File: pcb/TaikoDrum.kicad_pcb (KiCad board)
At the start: 2 copper layers, 50 x 45 mm, 34 parts, among them J1 USB_B_Micro, J2 Conn_02x04_Odd_Even, U1 STM32F103C8Tx, U3 LM358, U4 LM3940IMPX-3.3_NOPB, Y1 8Mhz

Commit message: Added docs. Modified README.
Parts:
- moved J1 0.18 mm to (105.0, 140.4)
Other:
- board text added: "GND"
- board text added: "P1"
- board text added: "P2"
- board text added: "P3"
- board text added: "P4"
- board text added: "SWCLK"
- board text added: "SWDIO"
- board text added: "VCC"

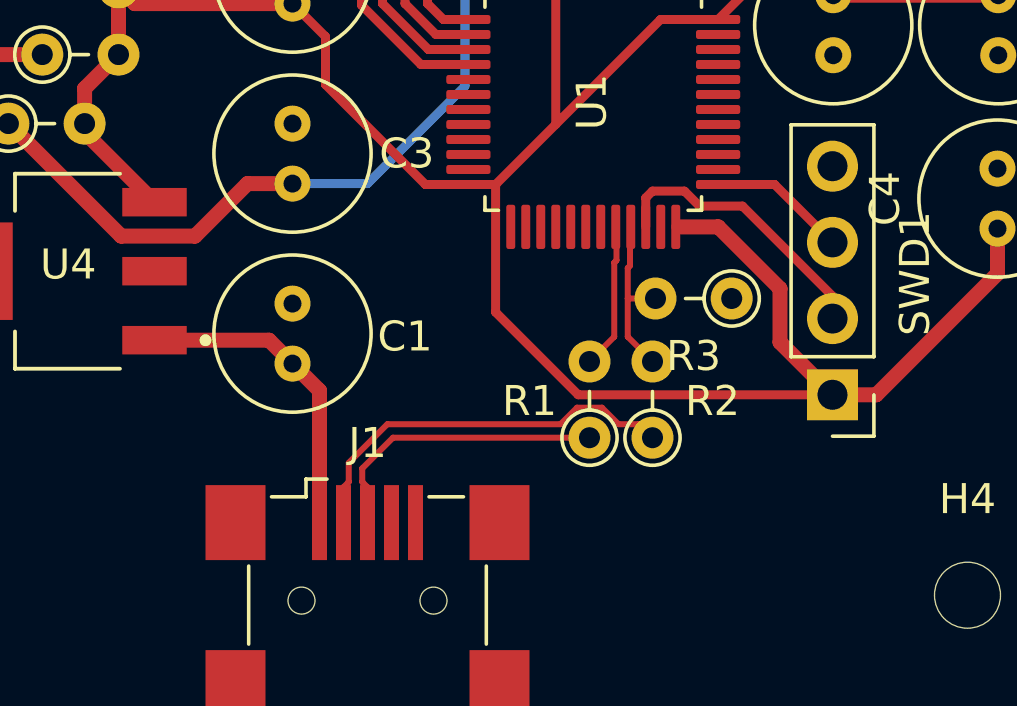
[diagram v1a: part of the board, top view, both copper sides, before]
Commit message: Fixed wrong USB wiring. Removed unecessary marks.
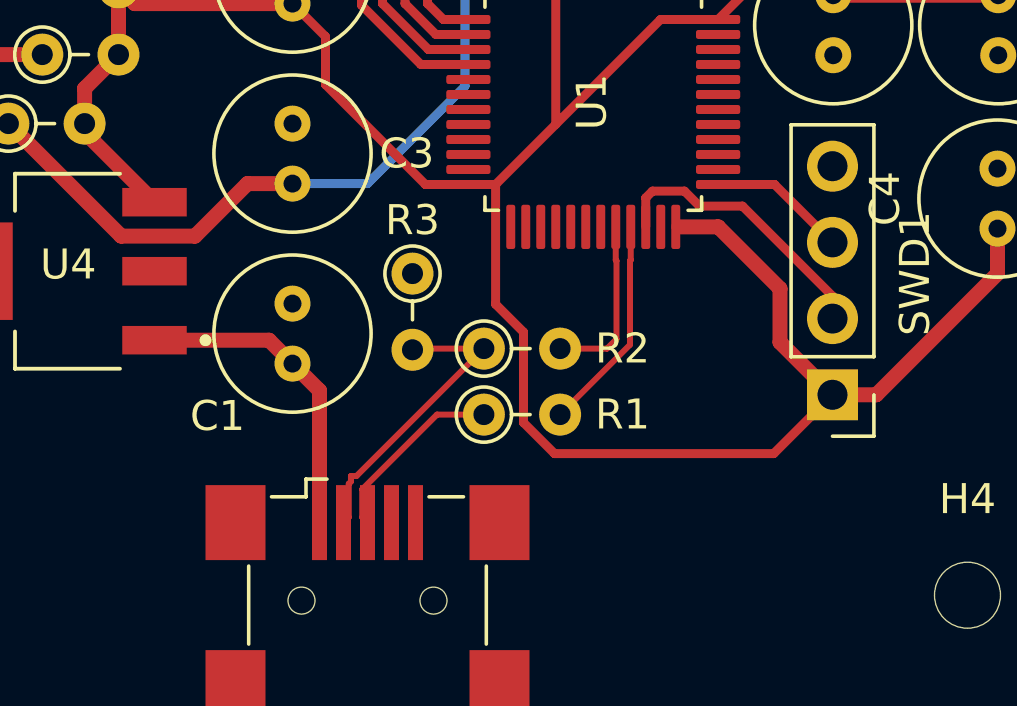
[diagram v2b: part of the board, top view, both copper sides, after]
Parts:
- R9: value 16M -> 1M
- moved R3 10.7 mm to (106.5, 129.5), turned to -90 degrees
- moved R2 6.36 mm to (108.9, 132.0), turned to 0 degrees
- moved R1 3.60 mm to (108.9, 134.2), turned to 0 degrees
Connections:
- U1 pad 32: D+ -> D-
- U1 pad 33: D- -> D+
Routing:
- net +3.3V: track 87.8 -> 91.0 mm
- net D-: track 19.0 -> 16.6 mm

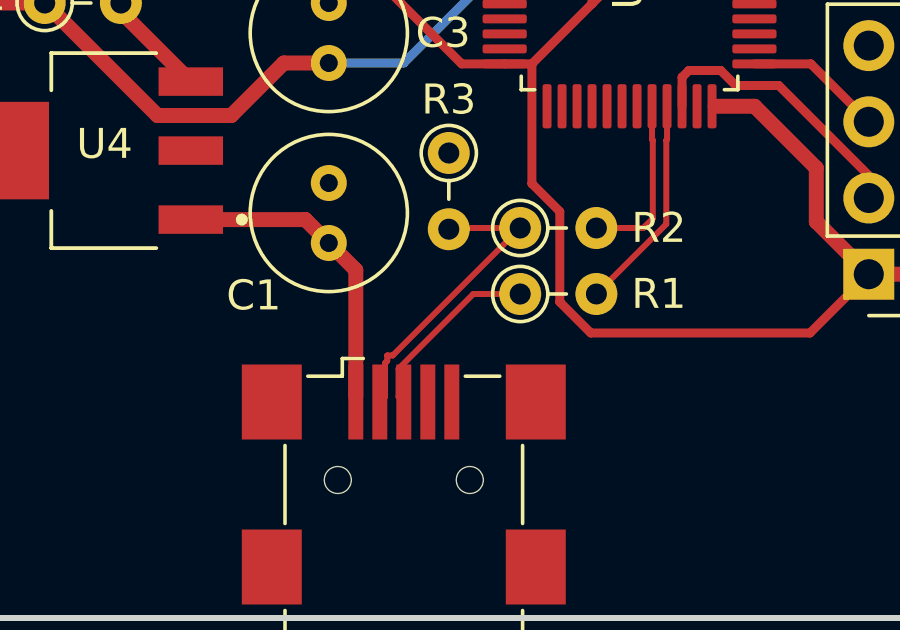
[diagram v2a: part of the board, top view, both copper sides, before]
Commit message: Better diff line routing. Additional dev text.
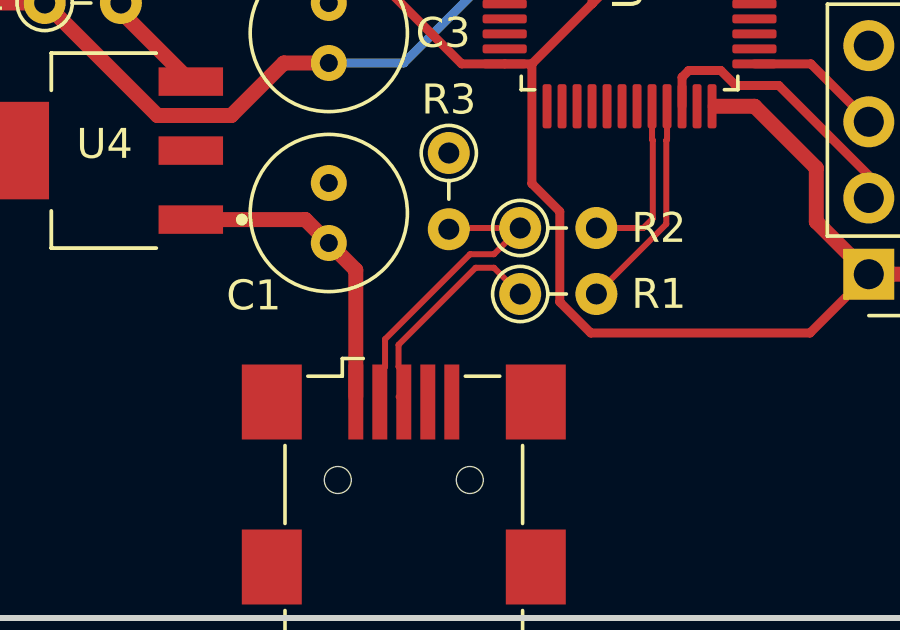
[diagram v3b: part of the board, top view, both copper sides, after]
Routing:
- net D+: track 14.1 -> 15.6 mm
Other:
- board text added: "USB-Micro-B"
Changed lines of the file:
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@@
 	)
 	(gr_text "VCC"
-		(at 125.2 134.1 0)
+		(at 118.6 134.2 0)
 		(layer "B.SilkS")
 		(effects
@@
 	)
 	(gr_text "SWDIO"
-		(at 126.8 129 0)
+		(at 118.6 129 0)
 		(layer "B.SilkS")
 		(effects
@@
 	)
 	(gr_text "GND"
-		(at 125.3 126.5 0)
+		(at 118.6 126.4 0)
 		(layer "B.SilkS")
 		(effects
@@
 	)
 	(gr_text "SWCLK"
-		(at 127.2 131.7 0)
+		(at 118.7 131.6 0)
+		(layer "B.SilkS")
+		(effects
+			(font
+				(size 1 1)
+				(thickness 0.1)
+			)
+			(justify left bottom mirror)
+		)
+	)
+	(gr_text "USB-Micro-B"
+		(at 110.2 143.2 0)
 		(layer "B.SilkS")
 		(effects
@@
 	)
 	(segment
+		(start 105 136.8)
+		(end 104.825 136.625)
+		(width 0.2)
+		(layer "F.Cu")
+		(net 9)
+	)
+	(segment
 		(start 113.75 129.073751)
 		(end 113.775 129.048751)
@@
 	)
 	(segment
-		(start 107.316397 134.2)
-		(end 108.88 134.2)
-		(width 0.2)
-		(layer "F.Cu")
-		(net 9)
-	)
-	(segment
 		(start 105 137.8)
 		(end 104.825001 137.625001)
@@
 	)
 	(segment
+		(start 105 137.8)
+		(end 105 136.8)
+		(width 0.2)
+		(layer "F.Cu")
+		(net 9)
+	)
+	(segment
+		(start 107.393197 133.325001)
+		(end 108.005001 133.325001)
+		(width 0.2)
+		(layer "F.Cu")
+		(net 9)
+	)
+	(segment
+		(start 108.005001 133.325001)
+		(end 108.88 134.2)
+		(width 0.2)
+		(layer "F.Cu")
+		(net 9)
+	)
+	(segment
+		(start 104.825 135.893198)
+		(end 107.393197 133.325001)
+		(width 0.2)
+		(layer "F.Cu")
+		(net 9)
+	)
+	(segment
 		(start 111.42 134.2)
 		(end 113.75 131.87)
@@
 	)
 	(segment
-		(start 104.825001 136.691396)
-		(end 107.316397 134.2)
-		(width 0.2)
-		(layer "F.Cu")
-		(net 9)
-	)
-	(segment
-		(start 104.825001 137.625001)
-		(end 104.825001 136.691396)
+		(start 104.825 136.625)
+		(end 104.825 135.893198)
 		(width 0.2)
 		(layer "F.Cu")
@@
 	)
 	(segment
+		(start 107.206803 132.874999)
+		(end 108.005001 132.874999)
+		(width 0.2)
+		(layer "F.Cu")
+		(net 34)
+	)
+	(segment
+		(start 104.2 137.8)
+		(end 104.2 136.8)
+		(width 0.2)
+		(layer "F.Cu")
+		(net 34)
+	)
+	(segment
+		(start 104.375 136.625)
+		(end 104.375 135.706802)
+		(width 0.2)
+		(layer "F.Cu")
+		(net 34)
+	)
+	(segment
 		(start 106.54 132)
 		(end 106.5 132.04)
@@
 	)
 	(segment
-		(start 104.374999 137.625001)
-		(end 104.374999 136.505001)
-		(width 0.2)
-		(layer "F.Cu")
-		(net 34)
-	)
-	(segment
 		(start 112.983603 132)
 		(end 113.3 131.683603)
@@
 	)
 	(segment
-		(start 104.449 136.431)
-		(end 104.449 136.249)
-		(width 0.2)
-		(layer "F.Cu")
-		(net 34)
-	)
-	(segment
 		(start 113.3 131.683603)
 		(end 113.3 129.073751)
@@
 	)
 	(segment
-		(start 104.374999 136.505001)
-		(end 104.449 136.431)
+		(start 108.005001 132.874999)
+		(end 108.88 132)
 		(width 0.2)
 		(layer "F.Cu")
@@
 	)
 	(segment
-		(start 104.449 136.249)
-		(end 104.631 136.249)
-		(width 0.2)
-		(layer "F.Cu")
-		(net 34)
-	)
-	(segment
 		(start 113.3 129.073751)
 		(end 113.275 129.048751)
@@
 	)
 	(segment
-		(start 104.2 137.8)
-		(end 104.374999 137.625001)
-		(width 0.2)
-		(layer "F.Cu")
-		(net 34)
-	)
-	(segment
 		(start 108.88 132)
 		(end 106.54 132)
@@
 	)
 	(segment
+		(start 104.375 135.706802)
+		(end 107.206803 132.874999)
+		(width 0.2)
+		(layer "F.Cu")
+		(net 34)
+	)
+	(segment
 		(start 113.275 128.53)
 		(end 113.3 128.555)
@@
 	)
 	(segment
-		(start 104.631 136.249)
-		(end 108.88 132)
-		(width 0.2)
-		(layer "F.Cu")
+		(start 104.2 136.8)
+		(end 104.375 136.625)
+		(width 0.2)
+		(layer "F.Cu")

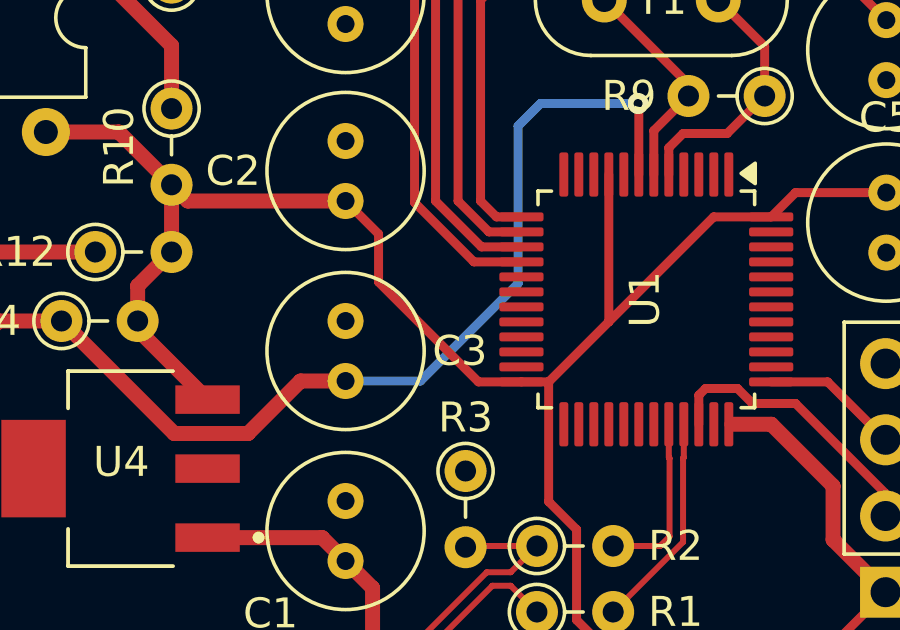
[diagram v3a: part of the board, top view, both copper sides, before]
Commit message: Fixed microcontroller GNDing.
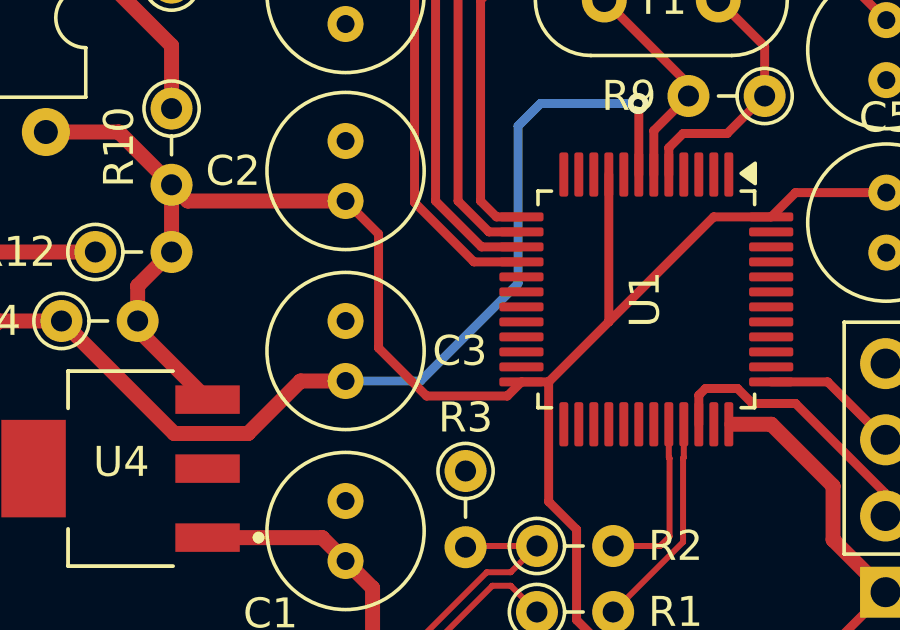
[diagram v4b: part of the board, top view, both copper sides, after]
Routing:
- net +3.3V: track 91.0 -> 92.7 mm
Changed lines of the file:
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@@
+	)
+	(segment
+		(start 110.2 134.466339)
+		(end 111.233661 135.5)
+		(width 0.3)
+		(layer "F.Cu")
+		(net 7)
+	)
+	(segment
+		(start 111.275 119.6175)
+		(end 111.275 124.525)
+		(width 0.3)
+		(layer "F.Cu")
+		(net 7)
+	)
+	(segment
+		(start 111.233661 135.5)
+		(end 118.54 135.5)
+		(width 0.3)
+		(layer "F.Cu")
+		(net 7)
+	)
+	(segment
+		(start 118.75 130)
+		(end 116.6925 127.9425)
+		(width 0.5)
+		(layer "F.Cu")
+		(net 7)
+	)
+	(segment
+		(start 116.6875 121.03)
+		(end 117.4975 120.22)
+		(width 0.3)
+		(layer "F.Cu")
+		(net 7)
+	)
+	(segment
+		(start 109.27 130.52)
+		(end 110.2 131.45)
+		(width 0.3)
+		(layer "F.Cu")
+		(net 7)
+	)
+	(segment
+		(start 97.24 120.5)
+		(end 96.7 119.96)
+		(width 0.5)
+		(layer "F.Cu")
+		(net 7)
+	)
+	(segment
+		(start 103.6 125.4)
+		(end 103.6 121.6)
+		(width 0.3)
+		(layer "F.Cu")
+		(net 7)
+	)
+	(segment
+		(start 105.2 127)
+		(end 103.6 125.4)
+		(width 0.3)
+		(layer "F.Cu")
+		(net 7)
+	)
+	(segment
+		(start 126.025 120.22)
+		(end 120.525 120.22)
+		(width 0.5)
+		(layer "F.Cu")
+		(net 7)
+	)
+	(segment
+		(start 116.6875 121.03)
+		(end 114.77 121.03)
+		(width 0.3)
+		(layer "F.Cu")
+		(net 7)
+	)
+	(segment
+		(start 118.54 135.5)
+		(end 120.5 133.54)
+		(width 0.3)
+		(layer "F.Cu")
+		(net 7)
+	)
+	(segment
+		(start 120.5 133.54)
+		(end 118.75 131.79)
+		(width 0.5)
+		(layer "F.Cu")
+		(net 7)
 	)
 	(segment
@@
 	)
 	(segment
-		(start 110.2 134.466339)
-		(end 111.233661 135.5)
-		(width 0.3)
-		(layer "F.Cu")
-		(net 7)
-	)
-	(segment
-		(start 111.275 119.6175)
-		(end 111.275 124.525)
-		(width 0.3)
-		(layer "F.Cu")
-		(net 7)
-	)
-	(segment
-		(start 111.233661 135.5)
-		(end 118.54 135.5)
-		(width 0.3)
-		(layer "F.Cu")
-		(net 7)
-	)
-	(segment
-		(start 118.75 130)
-		(end 116.6925 127.9425)
-		(width 0.5)
-		(layer "F.Cu")
-		(net 7)
-	)
-	(segment
-		(start 116.6875 121.03)
-		(end 117.4975 120.22)
-		(width 0.3)
-		(layer "F.Cu")
-		(net 7)
-	)
-	(segment
-		(start 108.3625 126.53)
-		(end 106.93 126.53)
-		(width 0.3)
-		(layer "F.Cu")
-		(net 7)
-	)
-	(segment
-		(start 109.27 130.52)
-		(end 110.2 131.45)
-		(width 0.3)
-		(layer "F.Cu")
-		(net 7)
-	)
-	(segment
-		(start 97.24 120.5)
-		(end 96.7 119.96)
-		(width 0.5)
-		(layer "F.Cu")
-		(net 7)
-	)
-	(segment
-		(start 103.6 123.2)
-		(end 103.6 121.6)
-		(width 0.3)
-		(layer "F.Cu")
-		(net 7)
-	)
-	(segment
-		(start 126.025 120.22)
-		(end 120.525 120.22)
-		(width 0.5)
-		(layer "F.Cu")
-		(net 7)
-	)
-	(segment
-		(start 116.6875 121.03)
-		(end 114.77 121.03)
-		(width 0.3)
-		(layer "F.Cu")
-		(net 7)
-	)
-	(segment
-		(start 118.54 135.5)
-		(end 120.5 133.54)
-		(width 0.3)
-		(layer "F.Cu")
-		(net 7)
-	)
-	(segment
-		(start 120.5 133.54)
-		(end 118.75 131.79)
-		(width 0.5)
-		(layer "F.Cu")
-		(net 7)
-	)
-	(segment
 		(start 126 129.5)
 		(end 121.96 133.54)
@@
 	)
 	(segment
-		(start 106.93 126.53)
-		(end 103.6 123.2)
-		(width 0.3)
-		(layer "F.Cu")
-		(net 7)
-	)
-	(segment
 		(start 95.57 124.5)
 		(end 95.57 123.33)
@@
 	)
 	(segment
+		(start 108.3625 126.53)
+		(end 107.8925 127)
+		(width 0.3)
+		(layer "F.Cu")
+		(net 7)
+	)
+	(segment
 		(start 92.51 118.2)
 		(end 94.94 118.2)
@@
 		(layer "F.Cu")
 		(net 7)
+	)
+	(segment
+		(start 107.8925 127)
+		(end 105.2 127)
+		(width 0.3)
+		(layer "F.Cu")
+		(net 7)

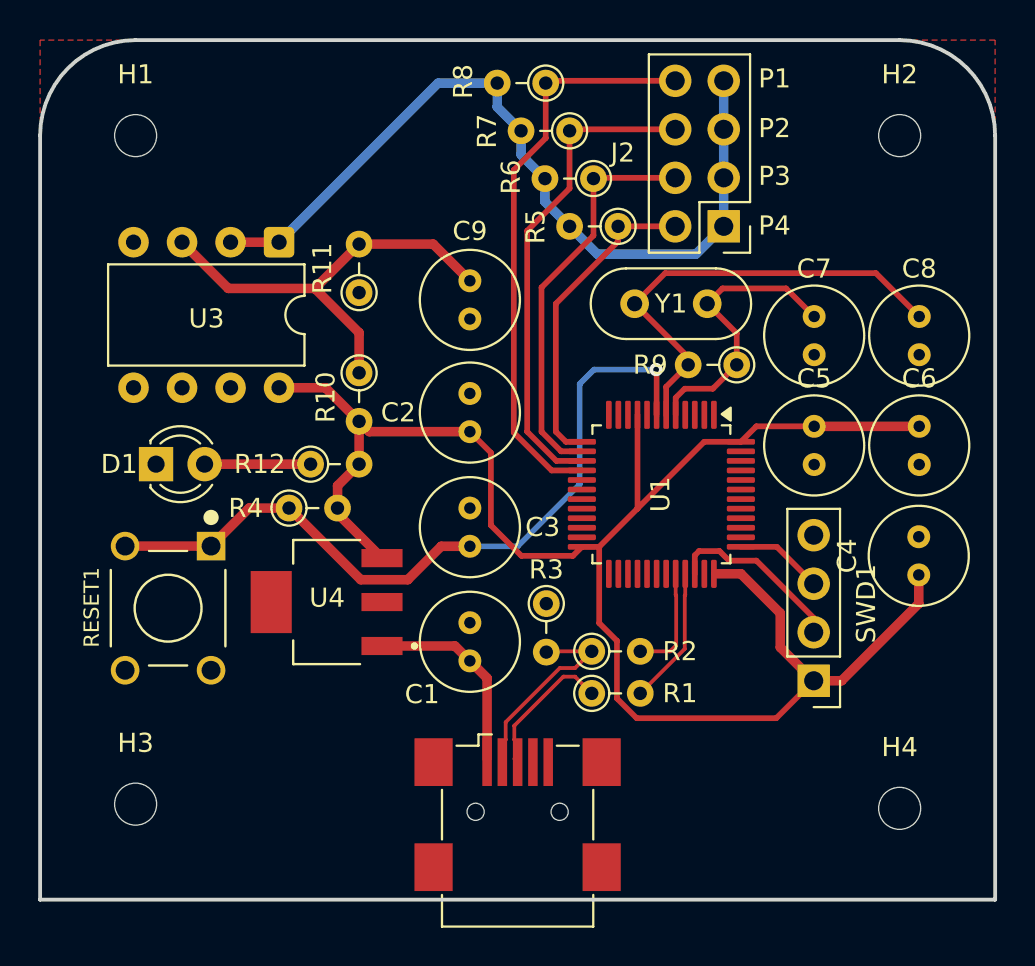
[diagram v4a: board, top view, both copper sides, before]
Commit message: Fixed all paths within the controller design. Swapped the micro USB footprint with JLCPCB compatible for auto assembly. Fixed clearance.
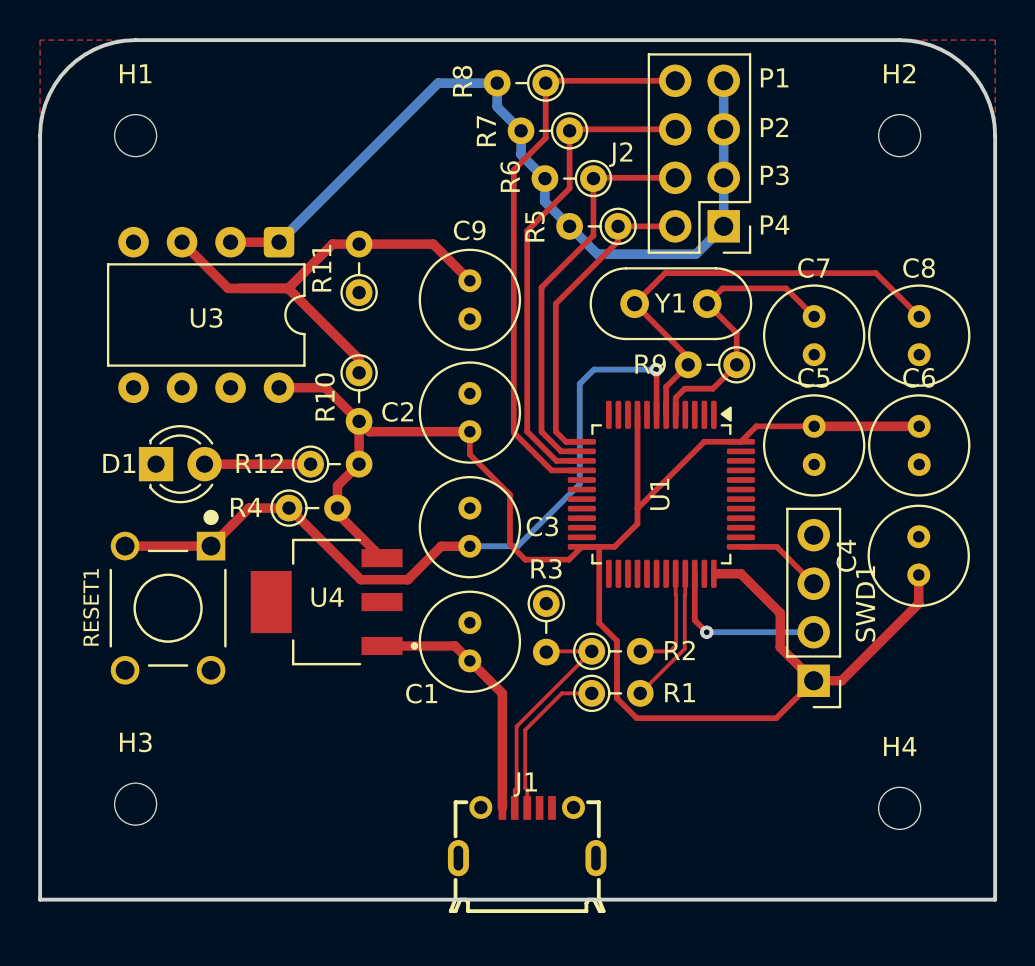
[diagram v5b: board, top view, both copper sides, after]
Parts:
- J1: footprint Connector_USB:USB_Mini-B_Wuerth_65100516121_Horizontal -> Library:MICRO-USB-SMD_5P-P0.65-H-F_C10418
- moved J1 1.21 mm to (105.5, 141.5)
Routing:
- net Net-(U3A-+): track 23.2 -> 26.4 mm
- net +5V: track 10.4 -> 13.3 mm
- net D-: track 17.0 -> 18.7 mm
- net D+: track 15.6 -> 16.3 mm
- net +3.3V: track 92.7 -> 93.4 mm
- net SWDIO: track 9.49 -> 8.92 mm, vias 0 -> 1
